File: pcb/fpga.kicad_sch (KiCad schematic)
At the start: 32 parts

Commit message: add footprints
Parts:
- C501: renamed from C?; footprint (none) -> Capacitor_SMD:C_1210_3225Metric_Pad1.33x2.70mm_HandSolder
- C503, C505, C506, C507, C509, C511, C512, C513, C514, C516, C518, C519, C520, C521, C522, C523, C524: renamed from C?; footprint (none) -> Capacitor_SMD:C_0805_2012Metric_Pad1.18x1.45mm_HandSolder
- R501, R502, R503, R504: renamed from R?; footprint Resistor_SMD:R_2512_6332Metric_Pad1.40x3.35mm_HandSolder -> Resistor_SMD:R_0805_2012Metric_Pad1.20x1.40mm_HandSolder
- gave numbers to parts that had none: 10

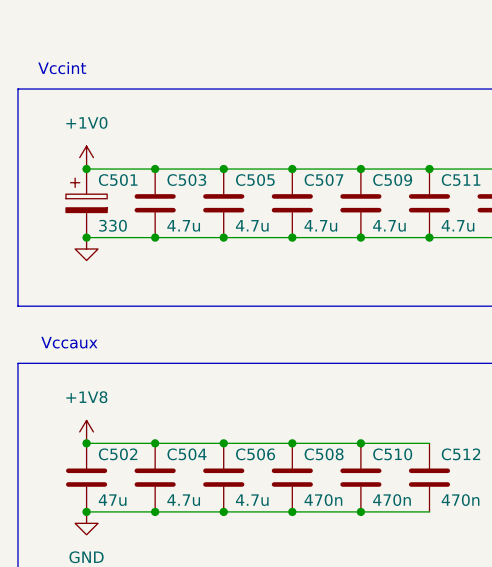
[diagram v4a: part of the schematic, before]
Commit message: connect onboard controller
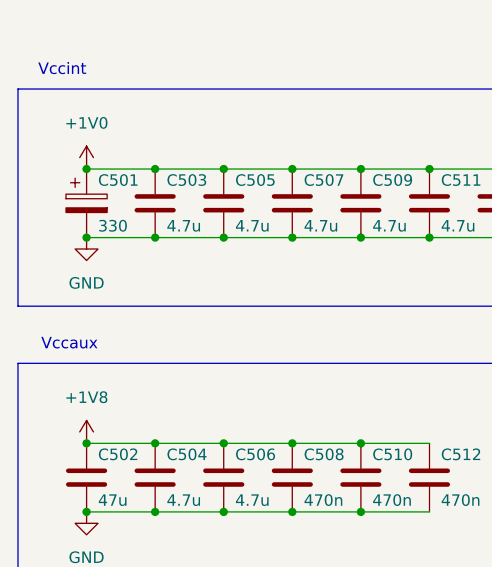
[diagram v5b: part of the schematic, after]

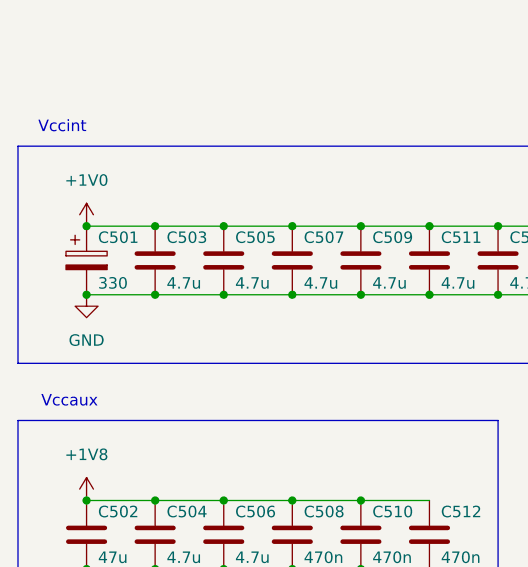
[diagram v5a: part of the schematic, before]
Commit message: fix capacitor values and footprints
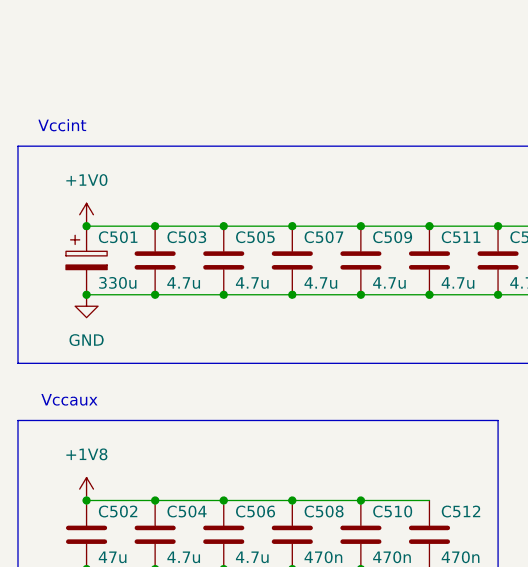
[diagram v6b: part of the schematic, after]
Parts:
- C501: value 330 -> 330u; footprint Capacitor_SMD:C_1210_3225Metric_Pad1.33x2.70mm_HandSolder -> 330uF:T520V337M2R5ATE025
- C502, C515: footprint Capacitor_SMD:C_0805_2012Metric_Pad1.18x1.45mm_HandSolder -> Capacitor_SMD:C_1210_3225Metric_Pad1.33x2.70mm_HandSolder
- C508, C510, C512, C514, C516, C517, C518, C519, C520, C521, C522, C523, C524: footprint Capacitor_SMD:C_0805_2012Metric_Pad1.18x1.45mm_HandSolder -> Capacitor_SMD:C_0603_1608Metric_Pad1.08x0.95mm_HandSolder
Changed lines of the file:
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@@
       (effects (font (size 1.27 1.27)) (justify left))
     )
-    (property "Footprint" "Capacitor_SMD:C_0805_2012Metric_Pad1.18x1.45mm_HandSolder" (id 2) (at 84.7852 151.13 0)
+    (property "Footprint" "Capacitor_SMD:C_0603_1608Metric_Pad1.08x0.95mm_HandSolder" (id 2) (at 84.7852 151.13 0)
       (effects (font (size 1.27 1.27)) hide)
     )
@@
       (effects (font (size 1.27 1.27)) (justify left))
     )
-    (property "Footprint" "Capacitor_SMD:C_0805_2012Metric_Pad1.18x1.45mm_HandSolder" (id 2) (at 61.9252 181.61 0)
+    (property "Footprint" "Capacitor_SMD:C_0603_1608Metric_Pad1.08x0.95mm_HandSolder" (id 2) (at 61.9252 181.61 0)
       (effects (font (size 1.27 1.27)) hide)
     )
@@
       (effects (font (size 1.27 1.27)) (justify left))
     )
-    (property "Footprint" "Capacitor_SMD:C_0805_2012Metric_Pad1.18x1.45mm_HandSolder" (id 2) (at 130.5052 151.13 0)
+    (property "Footprint" "Capacitor_SMD:C_0603_1608Metric_Pad1.08x0.95mm_HandSolder" (id 2) (at 130.5052 151.13 0)
       (effects (font (size 1.27 1.27)) hide)
     )
@@
       (effects (font (size 1.27 1.27)) (justify left))
     )
-    (property "Footprint" "Capacitor_SMD:C_0805_2012Metric_Pad1.18x1.45mm_HandSolder" (id 2) (at 138.1252 151.13 0)
+    (property "Footprint" "Capacitor_SMD:C_0603_1608Metric_Pad1.08x0.95mm_HandSolder" (id 2) (at 138.1252 151.13 0)
       (effects (font (size 1.27 1.27)) hide)
     )
@@
       (effects (font (size 1.27 1.27)) (justify left))
     )
-    (property "Footprint" "Capacitor_SMD:C_0805_2012Metric_Pad1.18x1.45mm_HandSolder" (id 2) (at 98.7552 181.61 0)
+    (property "Footprint" "Capacitor_SMD:C_0603_1608Metric_Pad1.08x0.95mm_HandSolder" (id 2) (at 98.7552 181.61 0)
       (effects (font (size 1.27 1.27)) hide)
     )
@@
       (effects (font (size 1.27 1.27)) (justify left))
     )
-    (property "Footprint" "Capacitor_SMD:C_0805_2012Metric_Pad1.18x1.45mm_HandSolder" (id 2) (at 92.4052 151.13 0)
+    (property "Footprint" "Capacitor_SMD:C_0603_1608Metric_Pad1.08x0.95mm_HandSolder" (id 2) (at 92.4052 151.13 0)
       (effects (font (size 1.27 1.27)) hide)
     )
@@
       (effects (font (size 1.27 1.27)) (justify left))
     )
-    (property "Footprint" "Capacitor_SMD:C_0805_2012Metric_Pad1.18x1.45mm_HandSolder" (id 2) (at 91.1352 181.61 0)
+    (property "Footprint" "Capacitor_SMD:C_1210_3225Metric_Pad1.33x2.70mm_HandSolder" (id 2) (at 91.1352 181.61 0)
       (effects (font (size 1.27 1.27)) hide)
     )
@@
       (effects (font (size 1.27 1.27)) (justify left))
     )
-    (property "Footprint" "Capacitor_SMD:C_0805_2012Metric_Pad1.18x1.45mm_HandSolder" (id 2) (at 107.6452 151.13 0)
+    (property "Footprint" "Capacitor_SMD:C_0603_1608Metric_Pad1.08x0.95mm_HandSolder" (id 2) (at 107.6452 151.13 0)
       (effects (font (size 1.27 1.27)) hide)
     )
@@
       (effects (font (size 1.27 1.27)) (justify left))
     )
-    (property "Footprint" "Capacitor_SMD:C_0805_2012Metric_Pad1.18x1.45mm_HandSolder" (id 2) (at 69.5452 181.61 0)
+    (property "Footprint" "Capacitor_SMD:C_0603_1608Metric_Pad1.08x0.95mm_HandSolder" (id 2) (at 69.5452 181.61 0)
       (effects (font (size 1.27 1.27)) hide)
     )
@@
       (effects (font (size 1.27 1.27)) (justify left))
     )
-    (property "Footprint" "Capacitor_SMD:C_0805_2012Metric_Pad1.18x1.45mm_HandSolder" (id 2) (at 115.2652 151.13 0)
+    (property "Footprint" "Capacitor_SMD:C_0603_1608Metric_Pad1.08x0.95mm_HandSolder" (id 2) (at 115.2652 151.13 0)
       (effects (font (size 1.27 1.27)) hide)
     )
@@
       (effects (font (size 1.27 1.27)) (justify left))
     )
-    (property "Value" "330" (id 1) (at 31.75 149.86 0)
-      (effects (font (size 1.27 1.27)) (justify left))
-    )
-    (property "Footprint" "Capacitor_SMD:C_1210_3225Metric_Pad1.33x2.70mm_HandSolder" (id 2) (at 31.4452 151.13 0)
+    (property "Value" "330u" (id 1) (at 31.75 149.86 0)
+      (effects (font (size 1.27 1.27)) (justify left))
+    )
+    (property "Footprint" "330uF:T520V337M2R5ATE025" (id 2) (at 31.4452 151.13 0)
       (effects (font (size 1.27 1.27)) hide)
     )
@@
       (effects (font (size 1.27 1.27)) (justify left))
     )
-    (property "Footprint" "Capacitor_SMD:C_0805_2012Metric_Pad1.18x1.45mm_HandSolder" (id 2) (at 122.8852 151.13 0)
+    (property "Footprint" "Capacitor_SMD:C_0603_1608Metric_Pad1.08x0.95mm_HandSolder" (id 2) (at 122.8852 151.13 0)
       (effects (font (size 1.27 1.27)) hide)
     )
@@
       (effects (font (size 1.27 1.27)) (justify left))
     )
-    (property "Footprint" "Capacitor_SMD:C_0805_2012Metric_Pad1.18x1.45mm_HandSolder" (id 2) (at 54.3052 181.61 0)
+    (property "Footprint" "Capacitor_SMD:C_0603_1608Metric_Pad1.08x0.95mm_HandSolder" (id 2) (at 54.3052 181.61 0)
       (effects (font (size 1.27 1.27)) hide)
     )
@@
       (effects (font (size 1.27 1.27)) (justify left))
     )
-    (property "Footprint" "Capacitor_SMD:C_0805_2012Metric_Pad1.18x1.45mm_HandSolder" (id 2) (at 100.0252 151.13 0)
+    (property "Footprint" "Capacitor_SMD:C_0603_1608Metric_Pad1.08x0.95mm_HandSolder" (id 2) (at 100.0252 151.13 0)
       (effects (font (size 1.27 1.27)) hide)
     )
@@
       (effects (font (size 1.27 1.27)) (justify left))
     )
-    (property "Footprint" "Capacitor_SMD:C_0805_2012Metric_Pad1.18x1.45mm_HandSolder" (id 2) (at 106.3752 181.61 0)
+    (property "Footprint" "Capacitor_SMD:C_0603_1608Metric_Pad1.08x0.95mm_HandSolder" (id 2) (at 106.3752 181.61 0)
       (effects (font (size 1.27 1.27)) hide)
     )
@@
       (effects (font (size 1.27 1.27)) (justify left))
     )
-    (property "Footprint" "Capacitor_SMD:C_0805_2012Metric_Pad1.18x1.45mm_HandSolder" (id 2) (at 31.4452 181.61 0)
-      (effects (font (size 1.27 1.27)) hide)
-    )
+    (property "Footprint" "Capacitor_SMD:C_1210_3225Metric_Pad1.33x2.70mm_HandSolder" (id 2) (at 31.4452 181.61 0)
+      (effects (font (size 1.27 1.27)) hide)
+    )
